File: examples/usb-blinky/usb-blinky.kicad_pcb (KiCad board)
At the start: 2 copper layers, 32 x 24 mm, 17 parts, among them J1 USB4105-GF-A, J2 ISP, SW1 TL3342, U1 AP2112K-3.3, U2 ATtiny85-20S

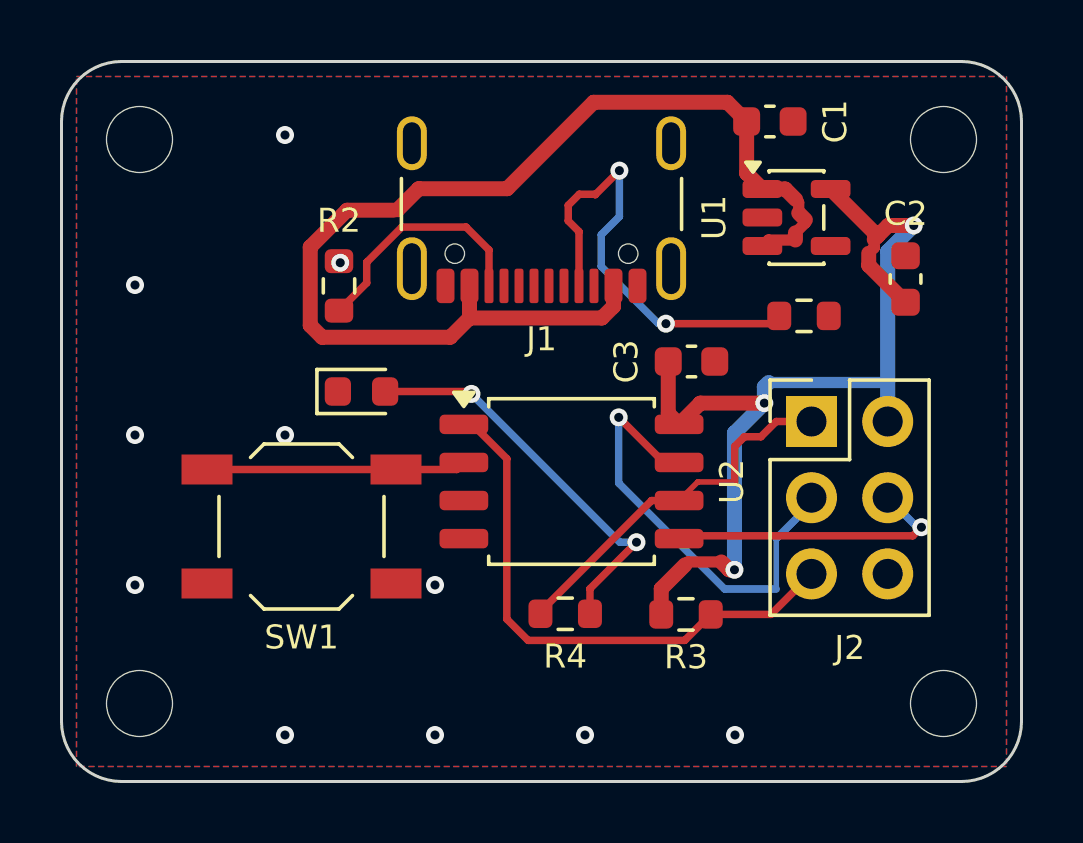
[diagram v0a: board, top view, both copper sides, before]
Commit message: Fix issues found by a cold test on a new board
- route: strip pour planes from the Specctra export so ground is routed as
  tracks; pads in pour islands cut off by signal traces were left stranded
- stitch: keep ground stitching vias out of pads (via-in-pad wicks solder)
- review: flag vias inside SMD pads as major
- board-figure, board_dump: create missing output folders
- figures: reserve headroom for the lifted pose so parts stay in the card;
  edge headers turn the camera like other edge connectors; quieter focus ring
- setup: note when KiCad's 3D models are missing
- docs: capture uses --theme (not --light), --zoom is in card px,
  placement 'at' is the footprint origin, unrouted is expected before
  routing, ground nets are not current-checked, a minimal complete spec
- examples regenerated with the fixed tools

Co-Authored-By: Claude Opus 5.5 <noreply@anthropic.com>
Claude-Session: https://claude.ai/code/session_01YQTWuTJTNHVLUEzL7EC4a5
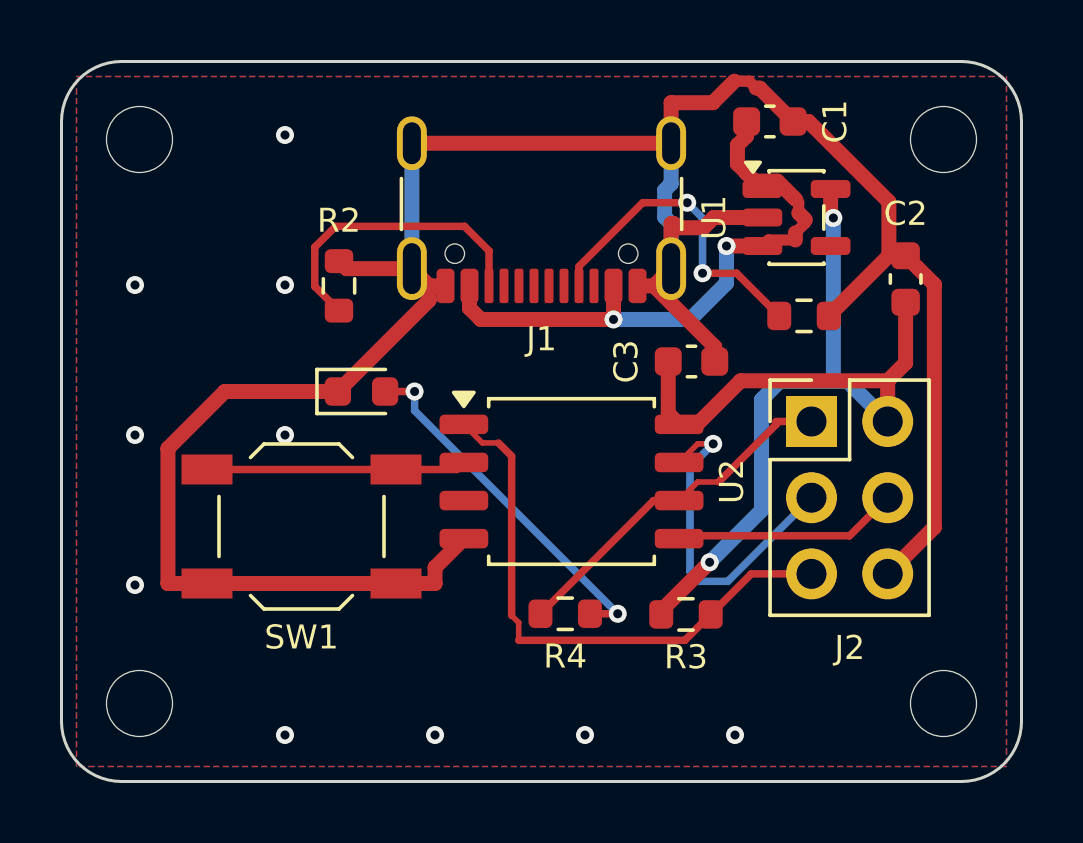
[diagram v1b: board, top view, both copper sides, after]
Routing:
- net GND: track 0.00 -> 84.5 mm, vias 11 -> 10
- net VBUS: track 38.4 -> 20.7 mm, vias 0 -> 2
- net /CC1: track 15.3 -> 10.8 mm
- net /SCK: track 15.1 -> 11.3 mm
- net /MOSI: track 9.77 -> 7.52 mm, vias 1 -> 0
- net /CC2: track 8.07 -> 10.1 mm
- net /LED_A: track 13.5 -> 12.1 mm
- net +3V3: track 33.1 -> 34.0 mm, vias 3 -> 2
- net /MISO: track 12.4 -> 11.7 mm
